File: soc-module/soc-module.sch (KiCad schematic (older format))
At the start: 17 parts, among them J1 Micro_SD, J2 East, J3 West, SW1 Prog, SW2 Reset, U1 ATECC608A-SSHDA, U2 ESP32-WROVER-IE-16MB

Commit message: Ongoing
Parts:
- removed J2: East, Connector_PinHeader_2.54mm:PinHeader_1x13_P2.54mm_Vertical, symbol Connector_Generic:Conn_01x13
- added J2: East, Connector_PinHeader_2.54mm:PinHeader_1x14_P2.54mm_Vertical, symbol Connector_Generic:Conn_01x14
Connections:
- net SPI_0_CLK is gone; now on net IO18: J1.5 (CLK), R4.1
- net SPI_0_MISO is gone; now on net IO19: J1.7 (DAT0), R3.1
- net SPI_0_MOSI is gone; now on net IO23: J1.3 (CMD), R5.1
- net GND: now also J2.1 (Pin_1)
- net I2C_SCL: now also J2.3 (Pin_3)
- net I2C_SDA: now also J2.6 (Pin_6)
- net IO0: now also J2.11 (Pin_11)
- net IO15: now also J2.13 (Pin_13)
- net IO18: now also J2.8 (Pin_8)
- net IO19: now also J2.7 (Pin_7)
- net IO2: now also J2.12 (Pin_12)
- net IO23: now also J2.2 (Pin_2)
- net IO4: now also J2.10 (Pin_10)
- net IO5: now also J2.9 (Pin_9)
- net U0RXD: now also J2.5 (Pin_5)
- net U0TXD: now also J2.4 (Pin_4)
- no-connect marks 4 -> 5
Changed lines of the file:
@@
 encoding utf-8
 Sheet 1 1
-Title ""
-Date ""
-Rev ""
-Comp ""
-Comment1 ""
+Title "Satellite SoM"
+Date "2021-12-01"
+Rev "2.0"
+Comp "GrayC GmbH"
+Comment1 "Fabian Schlegel"
 Comment2 ""
-Comment3 ""
-Comment4 ""
+Comment3 "ESP32-WROVER-IE, ATECC608A, µSD"
+Comment4 "Microcontroller with Crypto and Storage as single Module"
 $EndDescr
 $Comp
@@
 F 3 "~" H 10100 1850 50  0001 C CNN
 	1    10100 1850
-	1    0    0    -1
-$EndComp
-$Comp
-L Connector_Generic:Conn_01x13 J2
-U 1 1 6189476F
-P 10100 3350
-F 0 "J2" H 10180 3392 50  0000 L CNN
-F 1 "East" H 10180 3301 50  0000 L CNN
-F 2 "Connector_PinHeader_2.54mm:PinHeader_1x13_P2.54mm_Vertical" H 10100 3350 50  0001 C CNN
-F 3 "~" H 10100 3350 50  0001 C CNN
-	1    10100 3350
 	1    0    0    -1
 $EndComp
@@
 	0    1    1    0
 $EndComp
+$Comp
+L Connector_Generic:Conn_01x14 J2
+U 1 1 61A81BCC
+P 10100 3350
+F 0 "J2" H 10180 3342 50  0000 L CNN
+F 1 "East" H 10180 3251 50  0000 L CNN
+F 2 "Connector_PinHeader_2.54mm:PinHeader_1x14_P2.54mm_Vertical" H 10100 3350 50  0001 C CNN
+F 3 "~" H 10100 3350 50  0001 C CNN
+	1    10100 3350
+	1    0    0    -1
+$EndComp
+NoConn ~ 9650 4050
+Wire Wire Line
+	9650 4050 9900 4050
+Text GLabel 5250 6250 2    50   Input ~ 0
+IO23
+Text GLabel 5250 6400 2    50   Input ~ 0
+IO19
+Text GLabel 5250 6550 2    50   Input ~ 0
+IO18
+Wire Wire Line
+	5000 6250 5250 6250
+Wire Wire Line
+	5000 6400 5250 6400
+Wire Wire Line
+	5000 6550 5250 6550
 $EndSCHEMATC

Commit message: Ongoing Work. Still not ready for small and dedicated commits.
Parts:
- C1, C2, C3, C4: Price (none) -> 0.08; Product (none) -> https://www.mouser.de/ProductDetail/KEMET/C1206C104M5RACTU?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
- J1: Price (none) -> 2.19; Product (none) -> https://www.mouser.de/ProductDetail/Hirose-Connector/DM3AT-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
- J2, J3: Price (none) -> 1.10; Product (none) -> https://www.mouser.de/ProductDetail/Samtec/TSW-114-08-T-S?q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
- R1, R2, R3, R4, R5, R6: Price (none) -> 0.47; Product (none) -> https://www.mouser.de/ProductDetail/KOA-Speer/RN73H2BTTD100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
- SW1, SW2: Price (none) -> 0.48; Product (none) -> https://www.mouser.de/ProductDetail/CK/KMR231NGLFS?qs=%2Fha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
- U1: Price (none) -> 0.84; Product (none) -> https://www.mouser.de/ProductDetail/Microchip-Technology/AT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
- U2: Price (none) -> 3.26; Product (none) -> https://www.mouser.de/ProductDetail/Espressif-Systems/ESP32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
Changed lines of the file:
@@
 F 1 "ESP32-WROVER-IE-16MB" H 7025 4174 50  0000 C CNN
 F 2 "footprints:ESP32-WROVER" H 6400 4200 50  0001 C CNN
-F 3 "" H 6400 4200 50  0001 C CNN
+F 3 "https://www.mouser.de/datasheet/2/891/esp32_wrover_e_esp32_wrover_ie_datasheet_en-1855913.pdf" H 6400 4200 50  0001 C CNN
+F 4 "3.26" H 7050 2800 50  0001 C CNN "Price"
+F 5 "https://www.mouser.de/ProductDetail/Espressif-Systems/ESP32-WROVER-IEM213EH2864UH3Q0?qs=sGAEpiMZZMu3sxpa5v1qrgqRbH4gaXhhJoRXauER4Ss%3D" H 7050 2800 50  0001 C CNN "Product"
 	1    7050 2800
 	1    0    0    -1
@@
 F 2 "Package_SO:SOIC-8_3.9x4.9mm_P1.27mm" H 3950 1700 50  0001 C CNN
 F 3 "http://ww1.microchip.com/downloads/en/DeviceDoc/ATECC608A-CryptoAuthentication-Device-Summary-Data-Sheet-DS40001977B.pdf" H 4100 1950 50  0001 C CNN
+F 4 "0.84" H 3950 1700 50  0001 C CNN "Price"
+F 5 "https://www.mouser.de/ProductDetail/Microchip-Technology/ATECC608A-SSHDA-B?qs=wd5RIQLrsJj8ay8%2FHpTWlw%3D%3D" H 3950 1700 50  0001 C CNN "Product"
 	1    3950 1700
 	1    0    0    -1
@@
 F 1 "West" H 10180 1751 50  0000 L CNN
 F 2 "Connector_PinHeader_2.54mm:PinHeader_1x14_P2.54mm_Vertical" H 10100 1850 50  0001 C CNN
-F 3 "~" H 10100 1850 50  0001 C CNN
+F 3 "https://www.mouser.de/datasheet/2/527/tsw_th-2854687.pdf" H 10100 1850 50  0001 C CNN
+F 4 "1.10" H 10100 1850 50  0001 C CNN "Price"
+F 5 "https://www.mouser.de/ProductDetail/Samtec/TSW-114-08-T-S?qs=rU5fayqh%252BE0UYy2JFyXftg%3D%3D" H 10100 1850 50  0001 C CNN "Product"
 	1    10100 1850
 	1    0    0    -1
@@
 F 1 "100nF" V 5689 1350 50  0000 C CNN
 F 2 "Capacitor_SMD:C_1206_3216Metric_Pad1.33x1.80mm_HandSolder" H 5888 1200 50  0001 C CNN
-F 3 "~" H 5850 1350 50  0001 C CNN
+F 3 "https://www.mouser.de/datasheet/2/212/KEM_C1002_X7R_SMD-1102033.pdf" H 5850 1350 50  0001 C CNN
+F 4 "0.08" H 5850 1350 50  0001 C CNN "Price"
+F 5 "https://www.mouser.de/ProductDetail/KEMET/C1206C104M5RACTU?qs=sGAEpiMZZMsh%252B1woXyUXj6tIJRuySv4mnVhZeDkx3gA%3D" H 5850 1350 50  0001 C CNN "Product"
 	1    5850 1350
 	0    1    1    0
@@
 F 1 "100nF" V 5689 1800 50  0000 C CNN
 F 2 "Capacitor_SMD:C_1206_3216Metric_Pad1.33x1.80mm_HandSolder" H 5888 1650 50  0001 C CNN
-F 3 "~" H 5850 1800 50  0001 C CNN
+F 3 "https://www.mouser.de/datasheet/2/212/KEM_C1002_X7R_SMD-1102033.pdf" H 5850 1800 50  0001 C CNN
+F 4 "0.08" H 5850 1800 50  0001 C CNN "Price"
+F 5 "https://www.mouser.de/ProductDetail/KEMET/C1206C104M5RACTU?qs=sGAEpiMZZMsh%252B1woXyUXj6tIJRuySv4mnVhZeDkx3gA%3D" H 5850 1800 50  0001 C CNN "Product"
 	1    5850 1800
 	0    1    1    0
@@
 F 1 "100nF" H 3315 1655 50  0000 L CNN
 F 2 "Capacitor_SMD:C_1206_3216Metric_Pad1.33x1.80mm_HandSolder" H 3238 1550 50  0001 C CNN
-F 3 "~" H 3200 1700 50  0001 C CNN
+F 3 "https://www.mouser.de/datasheet/2/212/KEM_C1002_X7R_SMD-1102033.pdf" H 3200 1700 50  0001 C CNN
+F 4 "0.08" H 3200 1700 50  0001 C CNN "Price"
+F 5 "https://www.mouser.de/ProductDetail/KEMET/C1206C104M5RACTU?qs=sGAEpiMZZMsh%252B1woXyUXj6tIJRuySv4mnVhZeDkx3gA%3D" H 3200 1700 50  0001 C CNN "Product"
 	1    3200 1700
 	1    0    0    -1
@@
 F 1 "100nF" V 1389 3450 50  0000 C CNN
 F 2 "Capacitor_SMD:C_1206_3216Metric_Pad1.33x1.80mm_HandSolder" H 1588 3300 50  0001 C CNN
-F 3 "~" H 1550 3450 50  0001 C CNN
+F 3 "https://www.mouser.de/datasheet/2/212/KEM_C1002_X7R_SMD-1102033.pdf" H 1550 3450 50  0001 C CNN
+F 4 "0.08" H 1550 3450 50  0001 C CNN "Price"
+F 5 "https://www.mouser.de/ProductDetail/KEMET/C1206C104M5RACTU?qs=sGAEpiMZZMsh%252B1woXyUXj6tIJRuySv4mnVhZeDkx3gA%3D" H 1550 3450 50  0001 C CNN "Product"
 	1    1550 3450
 	0    1    1    0
@@
 F 1 "10k" V 1334 6850 50  0000 C CNN
 F 2 "Resistor_SMD:R_1206_3216Metric_Pad1.30x1.75mm_HandSolder" V 1380 6850 50  0001 C CNN
-F 3 "~" H 1450 6850 50  0001 C CNN
+F 3 "https://www.mouser.de/datasheet/2/219/RN73H-1843478.pdf" H 1450 6850 50  0001 C CNN
+F 4 "0.47" H 1450 6850 50  0001 C CNN "Price"
+F 5 "https://www.mouser.de/ProductDetail/KOA-Speer/RN73H2BTTD1002F100?qs=egkD4cx1ihTb7AhpW1EERA%3D%3D" H 1450 6850 50  0001 C CNN "Product"
 	1    1450 6850
 	0    1    1    0
@@
 F 1 "Prog" H 2100 6594 50  0000 C CNN
 F 2 "footprints:SW4SMD_63X161LS" H 2100 6600 50  0001 C CNN
-F 3 "" H 2100 6600 50  0001 C CNN
+F 3 "https://www.mouser.de/datasheet/2/60/kmr2-1841878.pdf" H 2100 6600 50  0001 C CNN
+F 4 "0.48" H 2100 6400 50  0001 C CNN "Price"
+F 5 "https://www.mouser.de/ProductDetail/CK/KMR231NGLFS?qs=%2Fha2pyFadug3C1LnpDTh3GC1%2FP5lYycwloRiMj1YBj0YTOPG2eMzYg%3D%3D" H 2100 6400 50  0001 C CNN "Product"
 	1    2100 6400
 	1    0    0    -1
@@
 F 1 "Reset" H 2100 7044 50  0000 C CNN
 F 2 "footprints:SW4SMD_63X161LS" H 2100 7050 50  0001 C CNN
-F 3 "" H 2100 7050 50  0001 C CNN
+F 3 "https://www.mouser.de/datasheet/2/60/kmr2-1841878.pdf" H 2100 7050 50  0001 C CNN
+F 4 "0.48" H 2100 6850 50  0001 C CNN "Price"
+F 5 "https://www.mouser.de/ProductDetail/CK/KMR231NGLFS?qs=%2Fha2pyFadug3C1LnpDTh3GC1%2FP5lYycwloRiMj1YBj0YTOPG2eMzYg%3D%3D" H 2100 6850 50  0001 C CNN "Product"
 	1    2100 6850
 	1    0    0    -1
@@
 F 1 "Micro_SD" H 2800 4776 50  0000 C CNN
 F 2 "Connector_Card:microSD_HC_Hirose_DM3AT-SF-PEJM5" H 4900 4750 50  0001 C CNN
-F 3 "https://www.hirose.com/product/en/download_file/key_name/DM3/category/Catalog/doc_file_id/49662/?file_category_id=4&item_id=195&is_series=1" H 2850 4150 50  0001 C CNN
+F 3 "https://www.mouser.de/datasheet/2/185/DM3AT_SF_PEJM5_CL0609_0031_0_00_2DDrawing_00009471-1614303.pdf" H 2850 4150 50  0001 C CNN
+F 4 "2.19" H 2850 4050 50  0001 C CNN "Price"
+F 5 "https://www.mouser.de/ProductDetail/Hirose-Connector/DM3AT-SF-PEJM5?qs=LZSZKJVF%252B2WTDKp%252BR7IYAQ%3D%3D" H 2850 4050 50  0001 C CNN "Product"
 	1    2850 4050
 	1    0    0    -1
@@
 F 1 "10k" V 1334 1350 50  0000 C CNN
 F 2 "Resistor_SMD:R_1206_3216Metric_Pad1.30x1.75mm_HandSolder" V 1380 1350 50  0001 C CNN
-F 3 "~" H 1450 1350 50  0001 C CNN
+F 3 "https://www.mouser.de/datasheet/2/219/RN73H-1843478.pdf" H 1450 1350 50  0001 C CNN
+F 4 "https://www.mouser.de/ProductDetail/KOA-Speer/RN73H2BTTD1002F100?qs=egkD4cx1ihTb7AhpW1EERA%3D%3D" V 1450 1350 50  0001 C CNN "Product"
+F 5 "0.47" V 1450 1350 50  0001 C CNN "Price"
 	1    1450 1350
 	0    1    1    0
@@
 F 1 "10k" V 1334 1700 50  0000 C CNN
 F 2 "Resistor_SMD:R_1206_3216Metric_Pad1.30x1.75mm_HandSolder" V 1380 1700 50  0001 C CNN
-F 3 "~" H 1450 1700 50  0001 C CNN
+F 3 "https://www.mouser.de/datasheet/2/219/RN73H-1843478.pdf" H 1450 1700 50  0001 C CNN
+F 4 "0.47" H 1450 1700 50  0001 C CNN "Price"
+F 5 "https://www.mouser.de/ProductDetail/KOA-Speer/RN73H2BTTD1002F100?qs=egkD4cx1ihTb7AhpW1EERA%3D%3D" H 1450 1700 50  0001 C CNN "Product"
 	1    1450 1700
 	0    1    1    0
@@
 F 1 "10k" V 1334 2050 50  0000 C CNN
 F 2 "Resistor_SMD:R_1206_3216Metric_Pad1.30x1.75mm_HandSolder" V 1380 2050 50  0001 C CNN
-F 3 "~" H 1450 2050 50  0001 C CNN
+F 3 "https://www.mouser.de/datasheet/2/219/RN73H-1843478.pdf" H 1450 2050 50  0001 C CNN
+F 4 "0.47" H 1450 2050 50  0001 C CNN "Price"
+F 5 "https://www.mouser.de/ProductDetail/KOA-Speer/RN73H2BTTD1002F100?qs=egkD4cx1ihTb7AhpW1EERA%3D%3D" H 1450 2050 50  0001 C CNN "Product"
 	1    1450 2050
 	0    1    1    0
@@
 F 1 "10k" V 1334 2400 50  0000 C CNN
 F 2 "Resistor_SMD:R_1206_3216Metric_Pad1.30x1.75mm_HandSolder" V 1380 2400 50  0001 C CNN
-F 3 "~" H 1450 2400 50  0001 C CNN
+F 3 "https://www.mouser.de/datasheet/2/219/RN73H-1843478.pdf" H 1450 2400 50  0001 C CNN
+F 4 "0.47" H 1450 2400 50  0001 C CNN "Price"
+F 5 "https://www.mouser.de/ProductDetail/KOA-Speer/RN73H2BTTD1002F100?qs=egkD4cx1ihTb7AhpW1EERA%3D%3D" H 1450 2400 50  0001 C CNN "Product"
 	1    1450 2400
 	0    1    1    0
@@
 F 1 "10k" V 1334 6400 50  0000 C CNN
 F 2 "Resistor_SMD:R_1206_3216Metric_Pad1.30x1.75mm_HandSolder" V 1380 6400 50  0001 C CNN
-F 3 "~" H 1450 6400 50  0001 C CNN
+F 3 "https://www.mouser.de/datasheet/2/219/RN73H-1843478.pdf" H 1450 6400 50  0001 C CNN
+F 4 "0.47" H 1450 6400 50  0001 C CNN "Price"
+F 5 "https://www.mouser.de/ProductDetail/KOA-Speer/RN73H2BTTD1002F100?qs=egkD4cx1ihTb7AhpW1EERA%3D%3D" H 1450 6400 50  0001 C CNN "Product"
 	1    1450 6400
 	0    1    1    0
@@
 F 1 "East" H 10180 3251 50  0000 L CNN
 F 2 "Connector_PinHeader_2.54mm:PinHeader_1x14_P2.54mm_Vertical" H 10100 3350 50  0001 C CNN
-F 3 "~" H 10100 3350 50  0001 C CNN
+F 3 "https://www.mouser.de/datasheet/2/527/tsw_th-2854687.pdf" H 10100 3350 50  0001 C CNN
+F 4 "1.10" H 10100 3350 50  0001 C CNN "Price"
+F 5 "https://www.mouser.de/ProductDetail/Samtec/TSW-114-08-T-S?qs=rU5fayqh%252BE0UYy2JFyXftg%3D%3D" H 10100 3350 50  0001 C CNN "Product"
 	1    10100 3350
 	1    0    0    -1

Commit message: Use a cheaper SD card interface
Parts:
- J1: footprint Connector_Card:microSD_HC_Hirose_DM3AT-SF-PEJM5 -> footprints:GCT_MEM2061-01-188-00-A_REVA
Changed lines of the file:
@@
 F 0 "J1" H 2800 4867 50  0000 C CNN
 F 1 "Micro_SD" H 2800 4776 50  0000 C CNN
-F 2 "Connector_Card:microSD_HC_Hirose_DM3AT-SF-PEJM5" H 4900 4750 50  0001 C CNN
+F 2 "footprints:GCT_MEM2061-01-188-00-A_REVA" H 4900 4750 50  0001 C CNN
 F 3 "https://www.mouser.de/datasheet/2/185/DM3AT_SF_PEJM5_CL0609_0031_0_00_2DDrawing_00009471-1614303.pdf" H 2850 4150 50  0001 C CNN
 F 4 "2.19" H 2850 4050 50  0001 C CNN "Price"

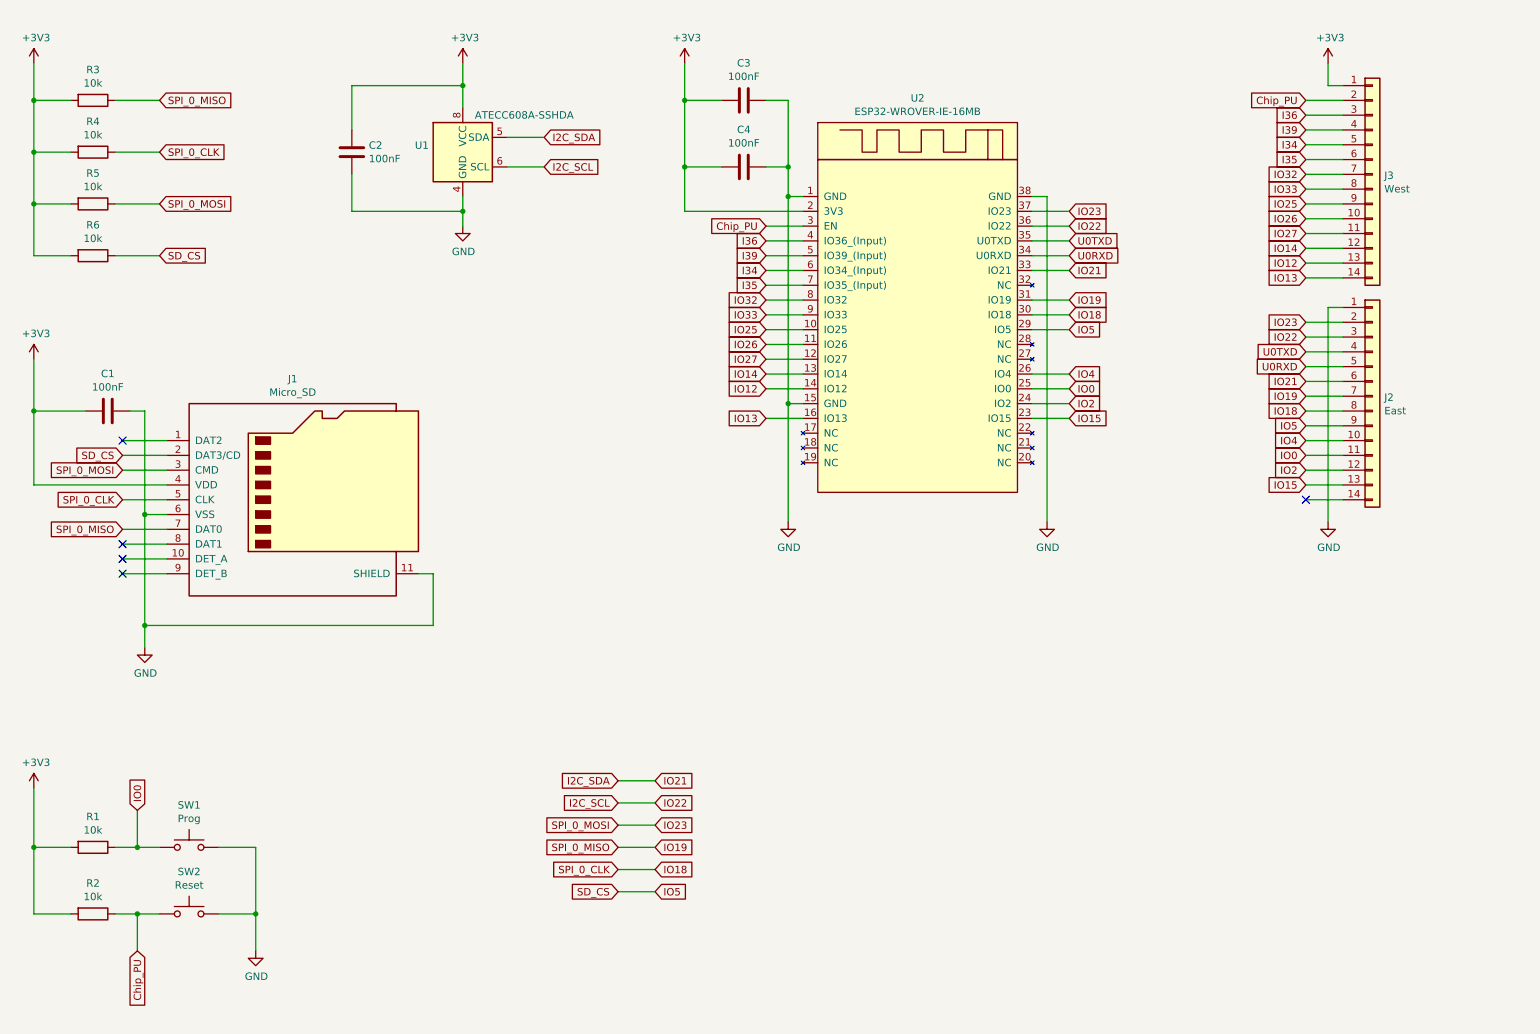
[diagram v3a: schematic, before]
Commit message: Work on Ethernet module
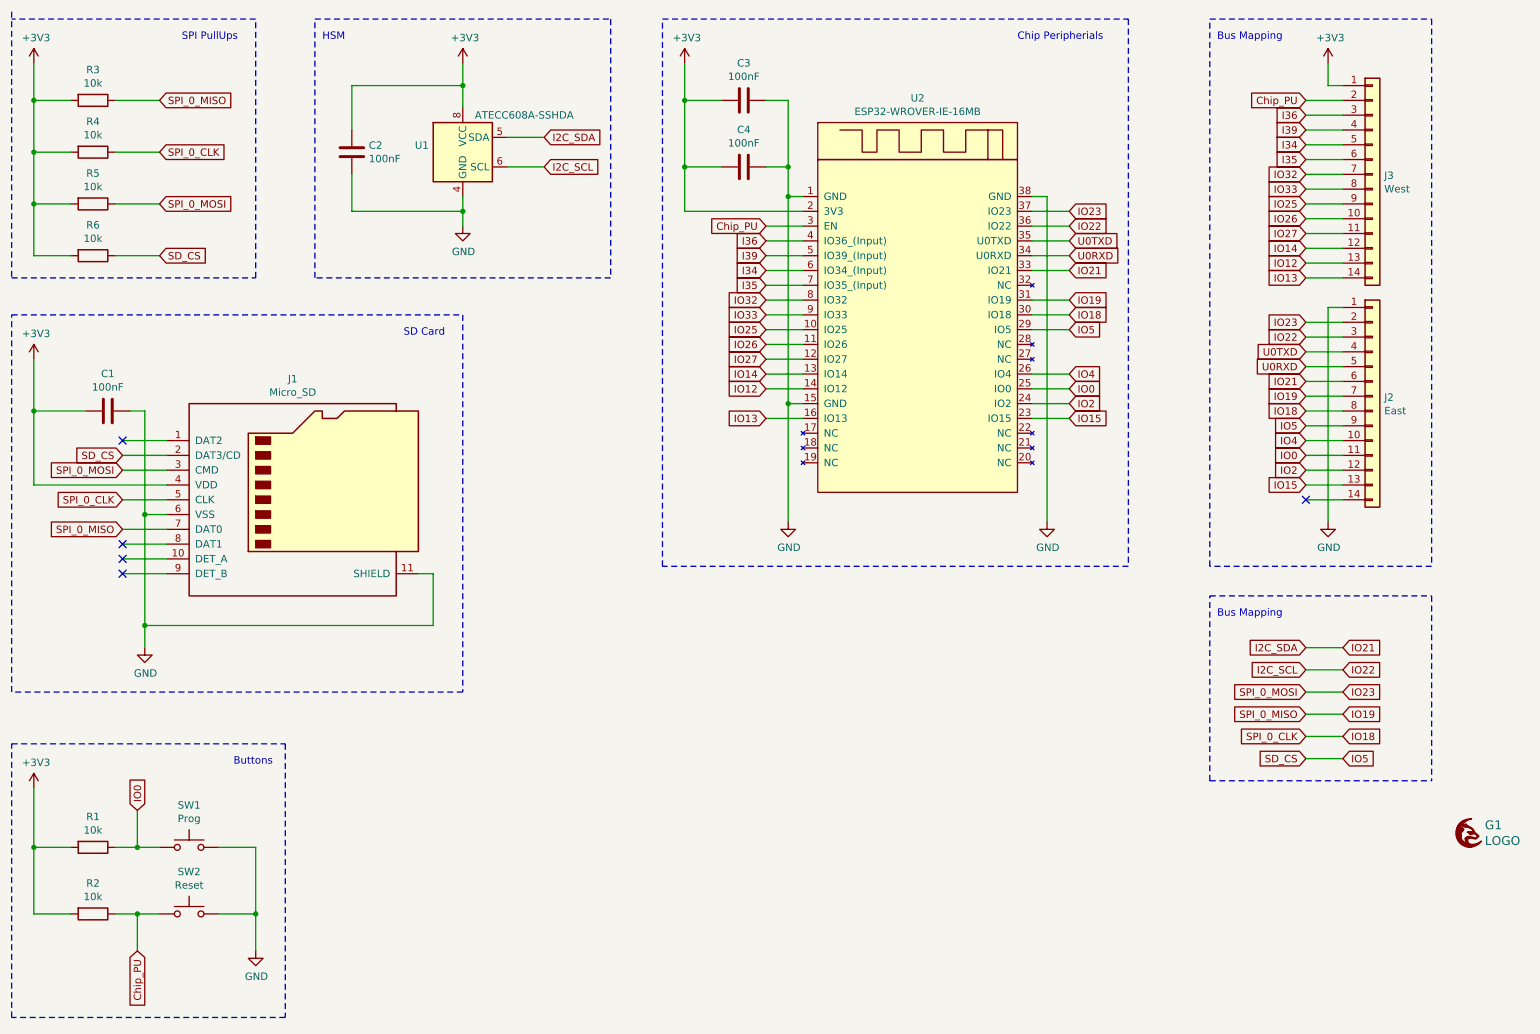
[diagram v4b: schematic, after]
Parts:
- added G1: LOGO, images:grayc-logo-negative, symbol grayc-logo-negative:LOGO
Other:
- note added: "Bus Mapping"
- note added: "Buttons"
- note added: "Chip Peripherials"
- note added: "HSM"
- note added: "SD Card"
- note added: "SPI PullUps"
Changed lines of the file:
@@
 Wire Wire Line
 	1800 4900 1800 5050
-Text GLabel 5000 5950 0    50   Input ~ 0
-I2C_SDA
-Text GLabel 5000 6100 0    50   Input ~ 0
-I2C_SCL
-Text GLabel 5000 6250 0    50   Input ~ 0
-SPI_0_MOSI
-Text GLabel 5000 6400 0    50   Input ~ 0
-SPI_0_MISO
-Text GLabel 5000 6550 0    50   Input ~ 0
-SPI_0_CLK
-Text GLabel 5000 6700 0    50   Input ~ 0
-SD_CS
-Text GLabel 5250 5950 2    50   Input ~ 0
-IO21
-Text GLabel 5250 6100 2    50   Input ~ 0
-IO22
-Text GLabel 5250 6700 2    50   Input ~ 0
-IO5
-Wire Wire Line
-	5000 5950 5250 5950
-Wire Wire Line
-	5250 6100 5000 6100
-Wire Wire Line
-	5000 6700 5250 6700
 $Comp
 L Device:R R1
@@
 Wire Wire Line
 	9650 4050 9900 4050
-Text GLabel 5250 6250 2    50   Input ~ 0
+Wire Wire Line
+	9650 5650 9900 5650
+Wire Wire Line
+	9650 5500 9900 5500
+Wire Wire Line
+	9650 5350 9900 5350
+Text GLabel 9900 5650 2    50   Input ~ 0
+IO18
+Text GLabel 9900 5500 2    50   Input ~ 0
+IO19
+Text GLabel 9900 5350 2    50   Input ~ 0
 IO23
-Text GLabel 5250 6400 2    50   Input ~ 0
-IO19
-Text GLabel 5250 6550 2    50   Input ~ 0
-IO18
 Wire Wire Line
-	5000 6250 5250 6250
+	9650 5800 9900 5800
 Wire Wire Line
-	5000 6400 5250 6400
+	9900 5200 9650 5200
 Wire Wire Line
-	5000 6550 5250 6550
+	9650 5050 9900 5050
+Text GLabel 9900 5800 2    50   Input ~ 0
+IO5
+Text GLabel 9900 5200 2    50   Input ~ 0
+IO22
+Text GLabel 9900 5050 2    50   Input ~ 0
+IO21
+Text GLabel 9650 5800 0    50   Input ~ 0
+SD_CS
+Text GLabel 9650 5650 0    50   Input ~ 0
+SPI_0_CLK
+Text GLabel 9650 5500 0    50   Input ~ 0
+SPI_0_MISO
+Text GLabel 9650 5350 0    50   Input ~ 0
+SPI_0_MOSI
+Text GLabel 9650 5200 0    50   Input ~ 0
+I2C_SCL
+Text GLabel 9650 5050 0    50   Input ~ 0
+I2C_SDA
+Text Notes 9050 4850 0    50   ~ 0
+Bus Mapping
+$Comp
+L grayc-logo-negative:LOGO G1
+U 1 1 6226A4CD
+P 10750 6300
+F 0 "G1" H 10860 6350 60  0000 L CNN
+F 1 "LOGO" H 10860 6244 60  0000 L CNN
+F 2 "images:grayc-logo-negative" H 10750 6300 50  0001 C CNN
+F 3 "" H 10750 6300 50  0001 C CNN
+	1    10750 6300
+	1    0    0    -1
+$EndComp
+Wire Notes Line
+	900  2550 2550 2550
+Wire Notes Line
+	2550 2550 2550 800
+Wire Notes Line
+	2550 800  900  800
+Wire Notes Line
+	900  750  900  2550
+Wire Notes Line
+	2950 800  4950 800
+Wire Notes Line
+	4950 800  4950 2550
+Wire Notes Line
+	4950 2550 2950 2550
+Wire Notes Line
+	2950 2550 2950 800
+Wire Notes Line
+	900  2800 3950 2800
+Wire Notes Line
+	3950 2800 3950 5350
+Wire Notes Line
+	3950 5350 900  5350
+Wire Notes Line
+	900  5350 900  2800
+Wire Notes Line
+	5300 800  8450 800
+Wire Notes Line
+	8450 800  8450 4500
+Wire Notes Line
+	8450 4500 5300 4500
+Wire Notes Line
+	5300 4500 5300 800
+Wire Notes Line
+	900  5700 2750 5700
+Wire Notes Line
+	2750 5700 2750 7550
+Wire Notes Line
+	2750 7550 900  7550
+Wire Notes Line
+	900  7550 900  5700
+Wire Notes Line
+	9000 800  10500 800
+Wire Notes Line
+	10500 800  10500 4500
+Wire Notes Line
+	10500 4500 9000 4500
+Wire Notes Line
+	9000 4500 9000 800
+Wire Notes Line
+	9000 5950 9000 4700
+Wire Notes Line
+	9000 4700 10500 4700
+Wire Notes Line
+	10500 4700 10500 5950
+Wire Notes Line
+	9000 5950 10500 5950
+Text Notes 7700 950  0    50   ~ 0
+Chip Peripherials
+Text Notes 9050 950  0    50   ~ 0
+Bus Mapping
+Text Notes 3000 950  0    50   ~ 0
+HSM
+Text Notes 2050 950  0    50   ~ 0
+SPI PullUps
+Text Notes 3550 2950 0    50   ~ 0
+SD Card
+Text Notes 2400 5850 0    50   ~ 0
+Buttons
 $EndSCHEMATC
